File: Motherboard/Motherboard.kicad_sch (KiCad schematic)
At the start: 57 parts, among them J1 40-pin IDE Connector, J3 Bus_ISA_8bit, J4 ATX-24, J5 USB_B, J6 ATF15XX_JTAG_ISP, J7 Bus_ISA_8bit, J8 65SIB_Connector, SW1 SW_Push, SW2 SW_SPST, U1 AS6C8008, U10 ATF1508AS-PLCC84, U11 74HCT245, U12 74HCT573, U13 8255, U14 WD65C22, U15 AS6C8008, U16 MCP2200-I-SO, U17 74HCT163, U18 LM7905_TO220, U19 GAL16V8, U2 74HCT04, U4 SST39SF040, U5 SST39SF040, U6 SST39SF040, U7 SST39SF040, U8 WD65C816S, U9 DS1813, X1 ACO-3.6864MHz, X2 ACO-24MHz, X3 ACO-14.31818MHz

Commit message: Fixed D7 line...
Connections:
- net D8 is gone; now on net D7: U11.9 (A7)
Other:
- moved on the sheet: J3

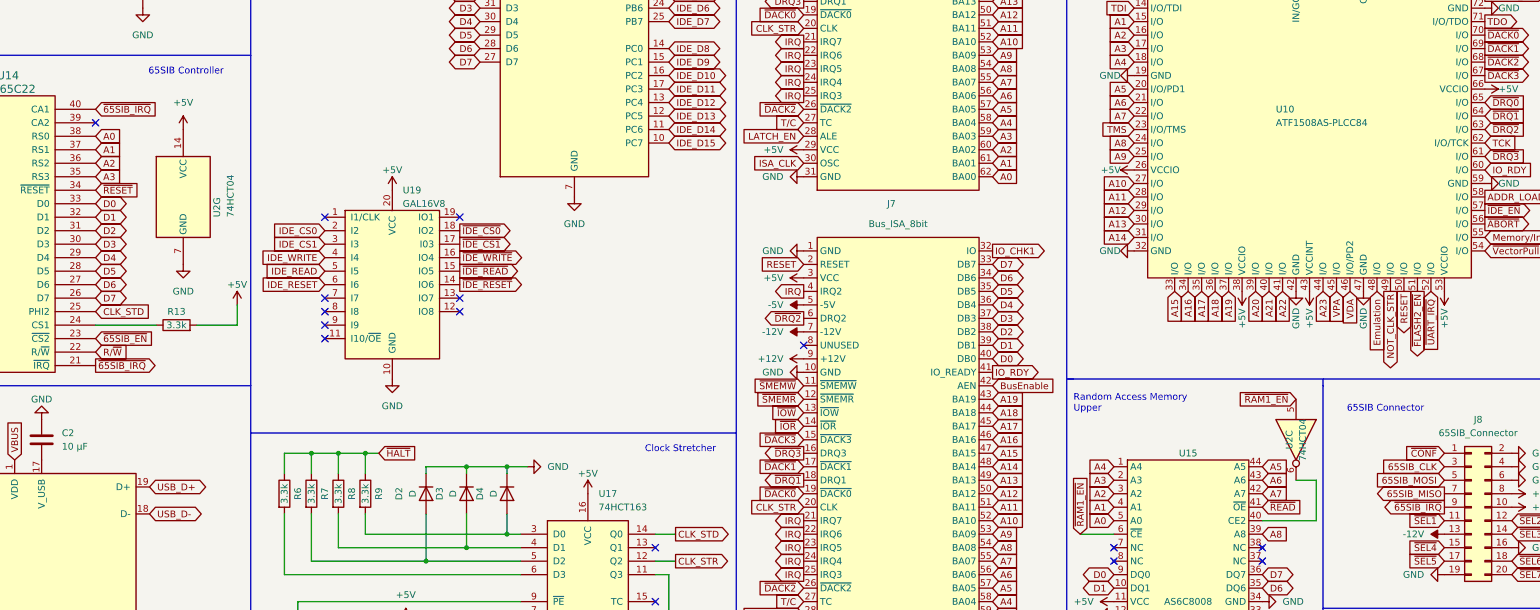
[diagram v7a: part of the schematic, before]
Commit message: 316 unrouted traces...
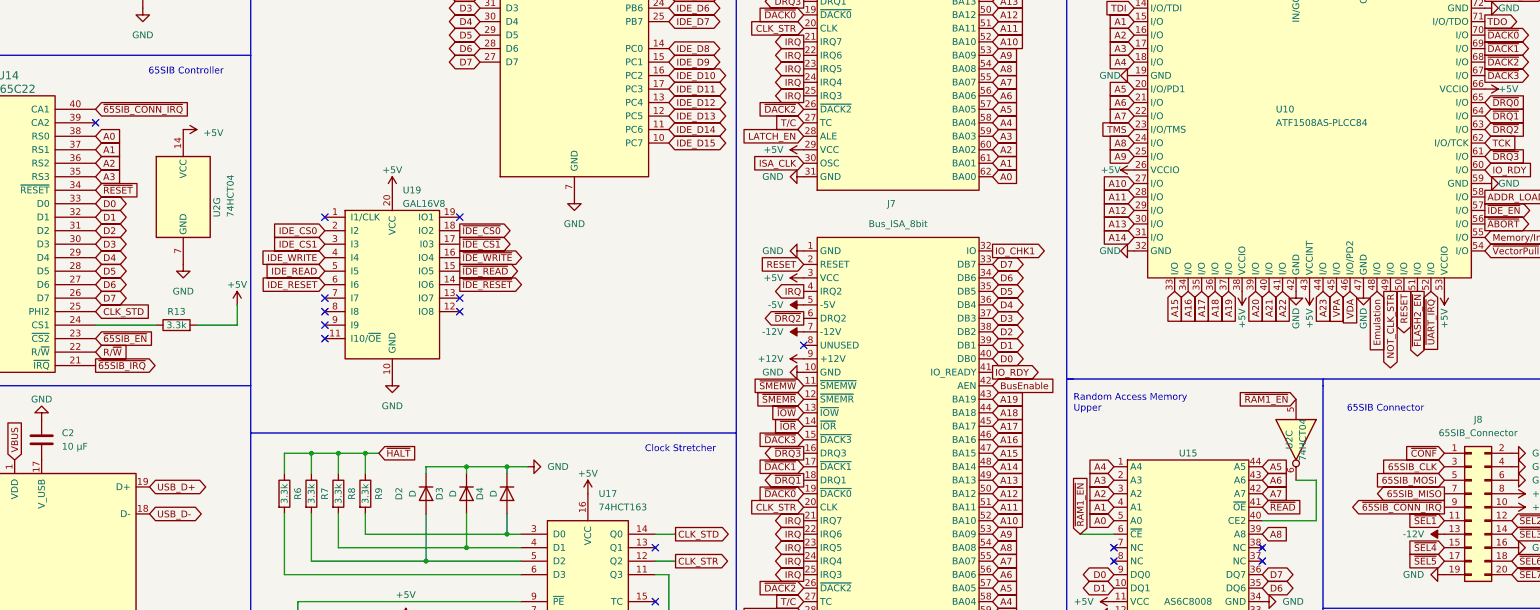
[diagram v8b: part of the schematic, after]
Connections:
- net ~{65SIB_IRQ}: no longer J8.9 (IRO\), U14.40 (CA1)
- new net ~{65SIB_CONN_IRQ}: J8.9 (IRO\), U14.40 (CA1)
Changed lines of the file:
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@@
     )
   )
-  (global_label "~{65SIB_IRQ}" (shape input) (at 175.26 217.17 0) (fields_autoplaced)
+  (global_label "~{65SIB_CONN_IRQ}" (shape input) (at 175.26 217.17 0) (fields_autoplaced)
     (effects (font (size 1.27 1.27)) (justify left))
-    (property "Intersheetrefs" "${INTERSHEET_REFS}" (at 187.3493 217.0906 0)
+    (property "Intersheetrefs" "${INTERSHEET_REFS}" (at 194.0711 217.17 0)
       (effects (font (size 1.27 1.27)) (justify left) hide)
     )
@@
     )
   )
-  (global_label "~{65SIB_IRQ}" (shape output) (at 429.26 292.1 180) (fields_autoplaced)
+  (global_label "~{65SIB_CONN_IRQ}" (shape output) (at 429.26 292.1 180) (fields_autoplaced)
     (effects (font (size 1.27 1.27)) (justify right))
-    (property "Intersheetrefs" "${INTERSHEET_REFS}" (at 417.1707 292.0206 0)
+    (property "Intersheetrefs" "${INTERSHEET_REFS}" (at 410.4489 292.1 0)
       (effects (font (size 1.27 1.27)) (justify right) hide)
     )
@@
     )
   )
-  (symbol (lib_id "power:+5V") (at 191.77 220.98 0) (unit 1)
+  (symbol (lib_id "power:+5V") (at 191.77 220.98 270) (unit 1)
     (in_bom yes) (on_board yes) (dnp no) (fields_autoplaced)
-    (property "Reference" "#PWR068" (at 191.77 224.79 0)
+    (property "Reference" "#PWR068" (at 187.96 220.98 0)
       (effects (font (size 1.27 1.27)) hide)
     )
-    (property "Value" "+5V" (at 191.77 215.9 0)
-      (effects (font (size 1.27 1.27)))
+    (property "Value" "+5V" (at 195.58 221.615 90)
+      (effects (font (size 1.27 1.27)) (justify left))
     )
     (property "Footprint" "" (at 191.77 220.98 0)
